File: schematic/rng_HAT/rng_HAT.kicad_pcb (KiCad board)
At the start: 2 copper layers, 56.5 x 65 mm, 38 parts, among them J1 RPi_GPIO, J2 Conn_01x04_Pin, Q1 2N3904, Q2 2N3904, Q3 2N3904, Q4 BC107, Q5 2N3904, U3 STM32F103C8Tx, Y2 8MHz

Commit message: PCB updates. holding  off on routes for now
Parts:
- added C10: 1uF, Capacitor_SMD:C_0603_1608Metric_Pad1.08x0.95mm_HandSolder, F.Cu at (182.4, 99.0)
- added C11: 220nF, Capacitor_SMD:C_0603_1608Metric_Pad1.08x0.95mm_HandSolder, F.Cu at (182.4, 96.0)
- added C12: 1nF, Capacitor_SMD:C_0603_1608Metric_Pad1.08x0.95mm_HandSolder, F.Cu at (182.5, 93.0)
- added C13: 220pF, Capacitor_SMD:C_0603_1608Metric_Pad1.08x0.95mm_HandSolder, F.Cu at (182.5, 90.1)
- added C9: 220nF, Capacitor_SMD:C_0603_1608Metric_Pad1.08x0.95mm_HandSolder, F.Cu at (182.5, 85.5)
- added D6: CLEAR(TX), LED_SMD:LED_0201_0603Metric, F.Cu at (191.5, 96.0)
- added R13: 2M, Resistor_SMD:R_0201_0603Metric, F.Cu at (185.8, 85.5)
- added R14: 10k, Resistor_SMD:R_0201_0603Metric, F.Cu at (185.9, 87.8)
- added R15: 1k, Resistor_SMD:R_0201_0603Metric, F.Cu at (185.8, 93.0)
- added R16: 47k, Resistor_SMD:R_0201_0603Metric, F.Cu at (185.9, 96.0)
- added R17: 200k, Resistor_SMD:R_0201_0603Metric, F.Cu at (185.9, 99.0)
- added R18: 4M7, Resistor_SMD:R_0201_0603Metric, F.Cu at (185.8, 90.0)
- added R19: 1k, Resistor_SMD:R_0201_0603Metric, F.Cu at (188.5, 96.0)
- added R20: 110, Resistor_SMD:R_0201_0603Metric, F.Cu at (188.5, 99.0)
- added U1: TL072CP, PCM_Package_DIP_AKL:DIP-8_W7.62mm_LongPads, F.Cu at (189.2, 85.9)
- moved D2 42.9 mm to (210.7, 98.5), turned to -90 degrees
- moved R3 41.2 mm to (208.7, 98.5), turned to 90 degrees
- moved R2 39.7 mm to (207.0, 98.5), turned to 90 degrees
- moved R4 39.1 mm to (211.2, 95.2), turned to -90 degrees
- moved R1 38.4 mm to (205.2, 98.5), turned to 90 degrees
- moved R5 37.1 mm to (209.2, 95.2), turned to -90 degrees
- moved D3 36.7 mm to (168.0, 96.5)
- moved R10 36.7 mm to (171.2, 96.5)
- moved R7 36.7 mm to (168.0, 99.0)
- moved C6 36.5 mm to (202.4, 98.5), turned to 180 degrees
- moved C1 35.5 mm to (207.2, 95.4), turned to -90 degrees
- moved C2 32.6 mm to (179.0, 85.9), turned to 90 degrees
- moved Q1 32.0 mm to (204.7, 92.5), turned to 180 degrees
- moved Q3 29.5 mm to (208.0, 91.4), turned to 0 degrees
- moved C4 28.8 mm to (169.5, 85.9), turned to -90 degrees
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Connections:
- U3 pad 31: unconnected-(U3-PA10-Pad31) -> Net-(U3-PA10)
- U3 pad 32: unconnected-(U3-PA11-Pad32) -> Net-(U3-PA11)

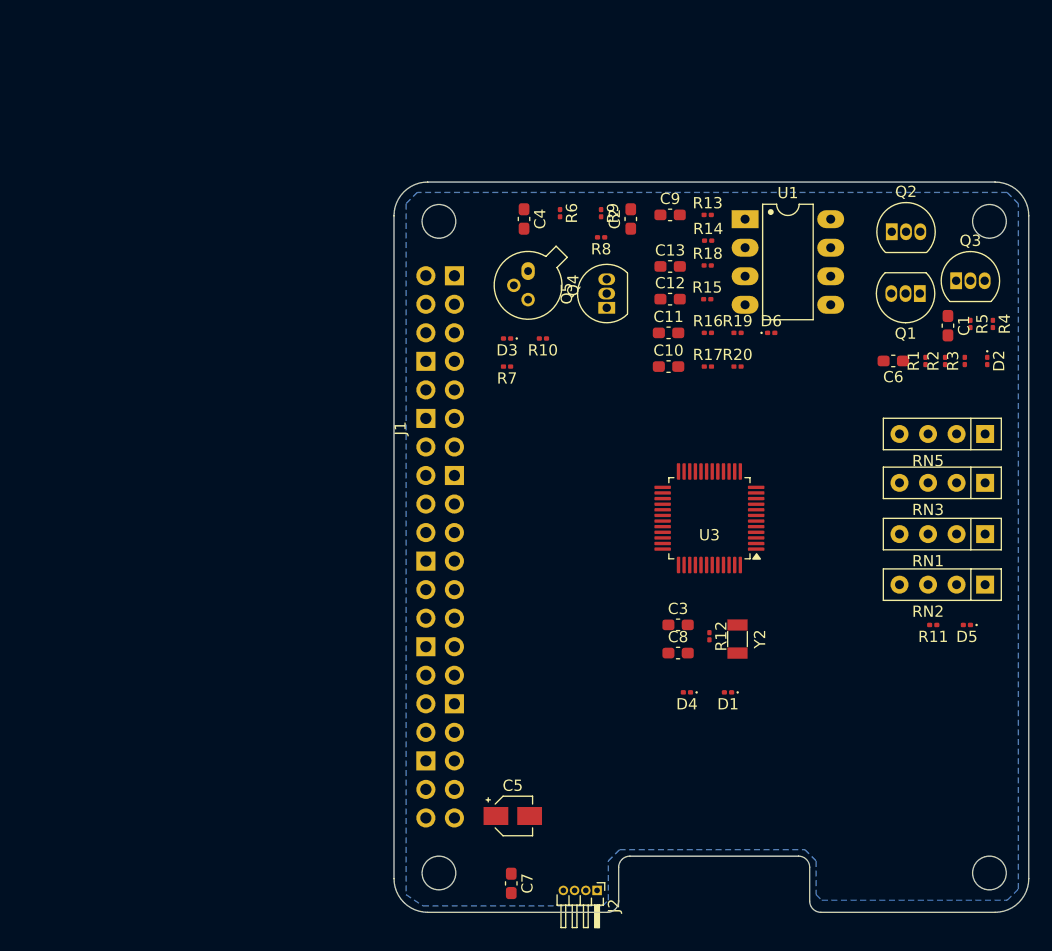
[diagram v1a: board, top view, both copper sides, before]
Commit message: PCB with traces. 2 errors, mostly warnings for cutoffs
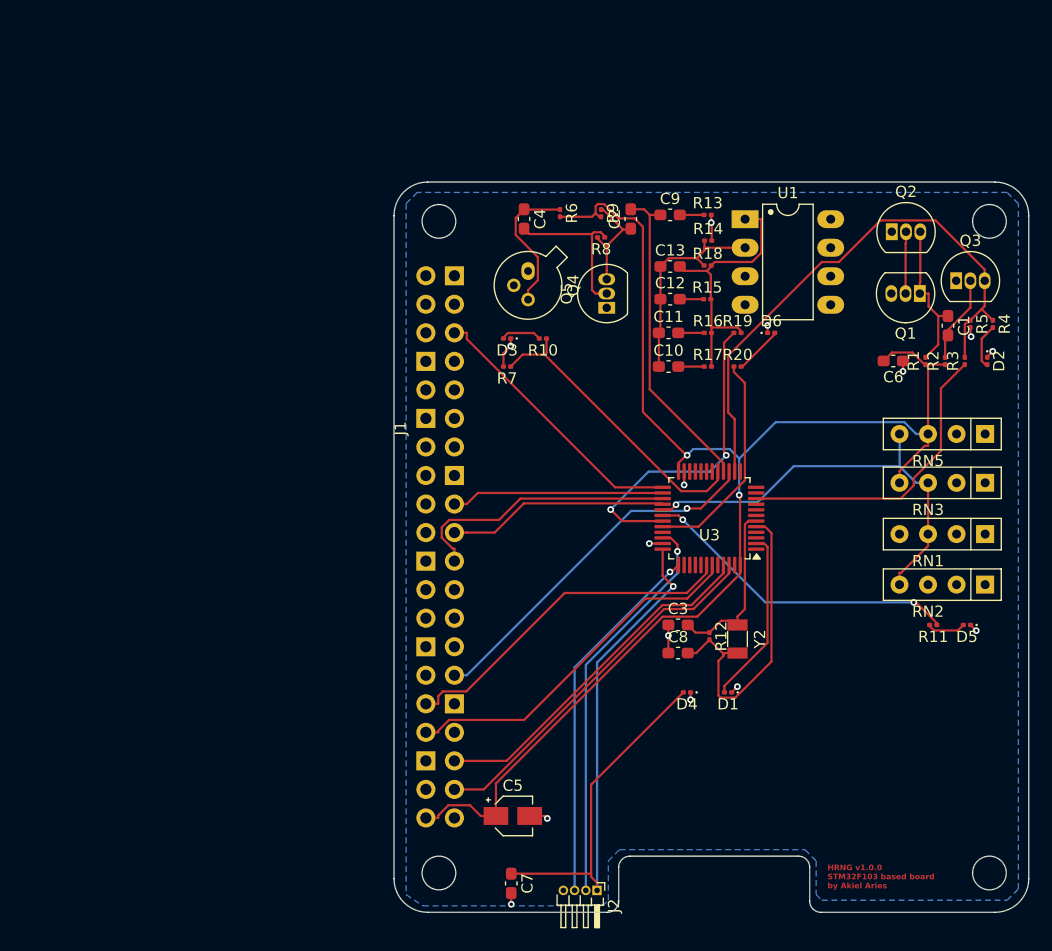
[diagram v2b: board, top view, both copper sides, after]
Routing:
- net 5V: track 0.00 -> 125.1 mm, vias 0 -> 2
- net 3V: track 0.00 -> 61.9 mm, vias 0 -> 1
- net AN LED: track 0.00 -> 50.2 mm
- net Net-(RN1-R2): track 0.00 -> 38.9 mm, vias 0 -> 1
- net Net-(J2-Pin_2): track 0.00 -> 35.7 mm, vias 0 -> 1
- net STRM I2C(DT): track 0.00 -> 33.2 mm
- net Net-(J2-Pin_3): track 0.00 -> 32.9 mm, vias 0 -> 1
- net RNG MUX: track 0.00 -> 32.4 mm, vias 0 -> 1
- net INTRPT?: track 0.00 -> 32.2 mm
- net STRM I2C(CLK): track 0.00 -> 31.6 mm
- net STREAM A: track 0.00 -> 30.9 mm
- net Net-(U3-PA10): track 0.00 -> 28.7 mm, vias 0 -> 2
- net Net-(U3-PA9): track 0.00 -> 28.5 mm, vias 0 -> 2
- net Net-(U3-PD0): track 0.00 -> 28.5 mm
- net WN OUT: track 0.00 -> 28.4 mm
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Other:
- board text added: "HRNG v1.0.0 STM32F103 based board by Akiel Aries"

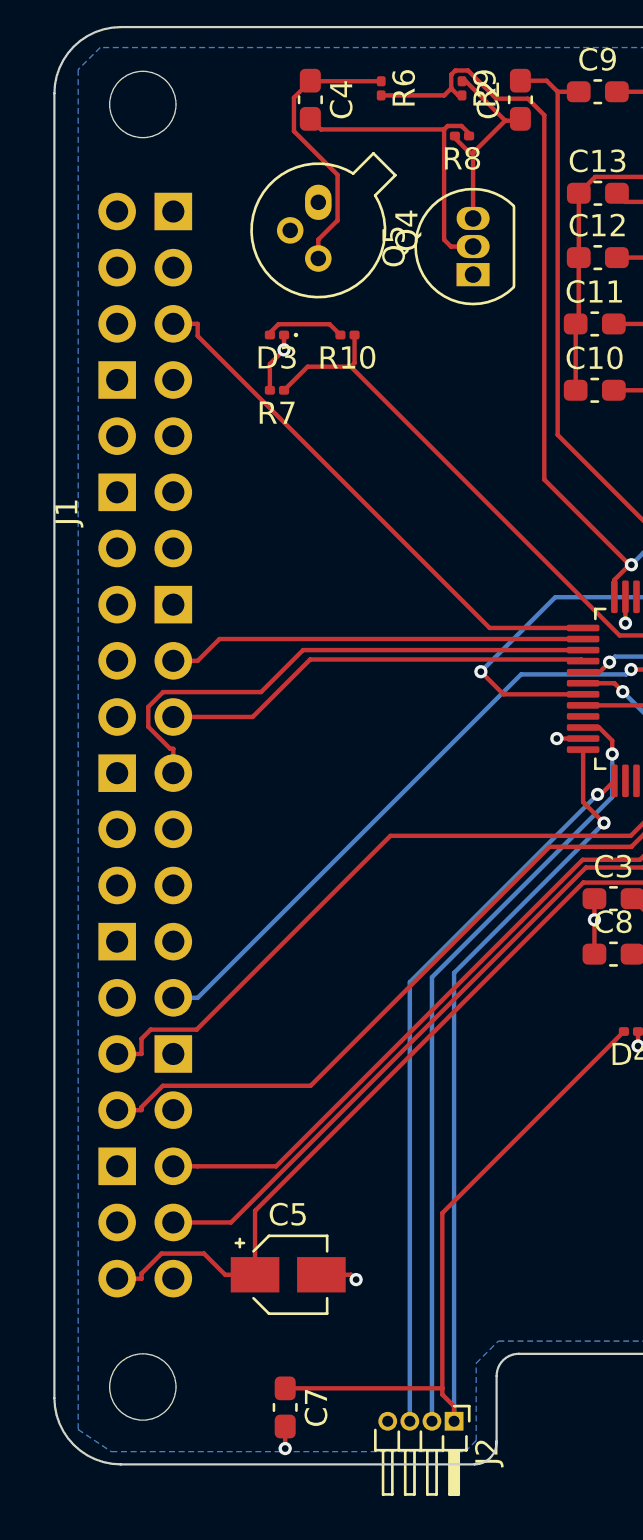
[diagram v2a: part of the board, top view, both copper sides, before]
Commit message: addressing some DRC warnings
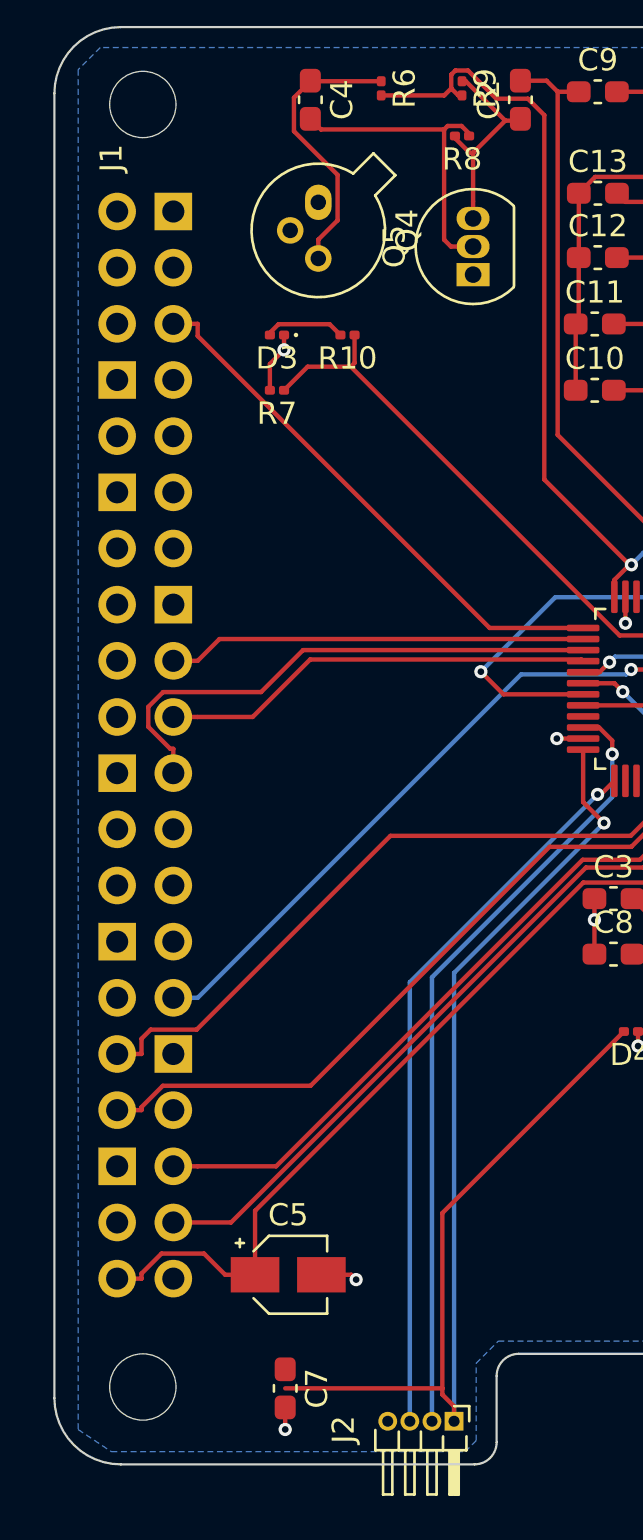
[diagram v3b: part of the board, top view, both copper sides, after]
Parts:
- moved C7 0.86 mm to (168.4, 144.1)
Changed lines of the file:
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@@
 		(at 161.925 115.075 90)
 		(property "Reference" "J1"
-			(at 10.575 -3.425 90)
+			(at 26.575 -1.425 90)
 			(unlocked yes)
 			(layer "F.SilkS")
@@
 		(tags "Through hole angled pin header THT 1x04 1.00mm single row")
 		(property "Reference" "J2"
-			(at 1.375 -1.5 90)
+			(at 0.375 5 90)
 			(layer "F.SilkS")
 			(effects
@@
 		)
 		(property "Value" "Conn_01x04_Pin"
-			(at 1.375 4.5 90)
+			(at -5.125 4 90)
 			(layer "F.Fab")
 			(effects
@@
 	(footprint "Capacitor_SMD:C_0603_1608Metric_Pad1.08x0.95mm_HandSolder"
 		(layer "F.Cu")
-		(at 168.3625 145 -90)
+		(at 168.3625 144.1375 -90)
 		(descr "Capacitor SMD 0603 (1608 Metric), square (rectangular) end terminal, IPC_7351 nominal with elongated pad for handsoldering. (Body size source: IPC-SM-782 page 76, https://www.pcb-3d.com/wordpress/wp-content/uploads/ipc-sm-782a_amendment_1_and_2.pdf), generated with kicad-footprint-generator")
 		(tags "capacitor handsolder")
@@
 		)
 		(property "Value" "104nF"
-			(at 0 1.43 90)
+			(at -0.5 1.43 90)
 			(layer "F.Fab")
 			(effects
@@
 	)
 	(segment
-		(start 168.3625 146.8584)
-		(end 168.3625 145.8625)
+		(start 168.3625 145.9959)
+		(end 168.3625 145)
 		(width 0.2)
 		(layer "F.Cu")
@@
 	)
 	(via
-		(at 168.3625 146.8584)
+		(at 168.3625 145.9959)
 		(size 0.6)
 		(drill 0.3)

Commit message: uhhh restarting traces and vias
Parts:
- moved J2 1.58 mm to (174.5, 145.1)
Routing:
- net 5V: track 125.1 -> 0.00 mm, vias 2 -> 0
- net 3V: track 61.9 -> 0.00 mm, vias 1 -> 0
- net AN LED: track 50.2 -> 0.00 mm
- net Net-(RN1-R2): track 38.9 -> 0.00 mm, vias 1 -> 0
- net Net-(J2-Pin_2): track 35.7 -> 0.00 mm, vias 1 -> 0
- net STRM I2C(DT): track 33.2 -> 0.00 mm
- net Net-(J2-Pin_3): track 32.9 -> 0.00 mm, vias 1 -> 0
- net RNG MUX: track 32.4 -> 0.00 mm, vias 1 -> 0
- net INTRPT?: track 32.2 -> 0.00 mm
- net STRM I2C(CLK): track 31.6 -> 0.00 mm
- net STREAM A: track 30.9 -> 0.00 mm
- net Net-(U3-PA10): track 28.7 -> 0.00 mm, vias 2 -> 0
- net Net-(U3-PA9): track 28.5 -> 0.00 mm, vias 2 -> 0
- net Net-(U3-PD0): track 28.5 -> 0.00 mm
- net WN OUT: track 28.4 -> 0.00 mm
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
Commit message: pics and readme?
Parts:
- moved U3 22.8 mm to (186.2, 135.3), turned to 90 degrees
- moved C3 21.7 mm to (200.2, 135.5)
- moved C8 21.7 mm to (200.2, 138.0)
- moved R12 21.7 mm to (203.0, 136.5)
- moved Y2 21.7 mm to (205.5, 136.8)
- moved D1 21.4 mm to (204.7, 141.0)
- moved D4 21.4 mm to (201.0, 141.0)
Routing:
- net 5V: track 0.00 -> 129.2 mm, vias 0 -> 2
- net WN OUT: track 0.00 -> 59.3 mm
- net AN LED: track 0.00 -> 56.4 mm
- net 3V: track 0.00 -> 55.3 mm, vias 0 -> 1
- net Net-(U3-PA9): track 0.00 -> 53.8 mm
- net AN OUT: track 0.00 -> 52.1 mm
- net WN LED: track 0.00 -> 51.2 mm
- net Net-(RN1-R2): track 0.00 -> 50.7 mm
- net CS: track 0.00 -> 45.9 mm
- net Net-(U3-PA10): track 0.00 -> 36.1 mm, vias 0 -> 2
- net STRM SPI(MISO): track 0.00 -> 35.6 mm
- net Net-(J1-BCM11_SCLK): track 0.00 -> 34.2 mm
- net Net-(U3-PA11): track 0.00 -> 33.5 mm, vias 0 -> 2
- net STRM SPI(MOSI): track 0.00 -> 31.6 mm
- net RNG MUX: track 0.00 -> 31.5 mm, vias 0 -> 1
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
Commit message: readme
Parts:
- moved C3 35.9 mm to (167.2, 121.5)
- moved C10 35.9 mm to (149.3, 85.0)
- moved C11 35.9 mm to (149.3, 82.0)
- moved C13 35.9 mm to (149.5, 76.1)
- moved C6 35.9 mm to (169.3, 84.5)
- moved C7 35.9 mm to (135.3, 130.1)
- moved C8 35.9 mm to (167.2, 124.0)
- moved D3 35.9 mm to (135.0, 82.5)
- moved J1 35.9 mm to (128.9, 101.0)
- moved Q3 35.9 mm to (174.9, 77.3)
- moved Q4 35.9 mm to (136.8, 76.5)
- moved Q5 35.9 mm to (143.8, 79.7)
- moved R10 35.9 mm to (138.2, 82.5)
- moved R16 35.9 mm to (152.8, 82.0)
- moved R17 35.9 mm to (152.8, 85.0)
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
